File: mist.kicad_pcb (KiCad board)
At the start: 2 copper layers, 137 x 110 mm, 25 parts, among them SW1 SW_Push, SW10 SW_Push, SW11 SW_Push, SW12 SW_Push, SW13 SW_Push, SW14 SW_Push, SW15 SW_Push, SW16 SW_Push, SW17 SW_Push, SW18 SW_Push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

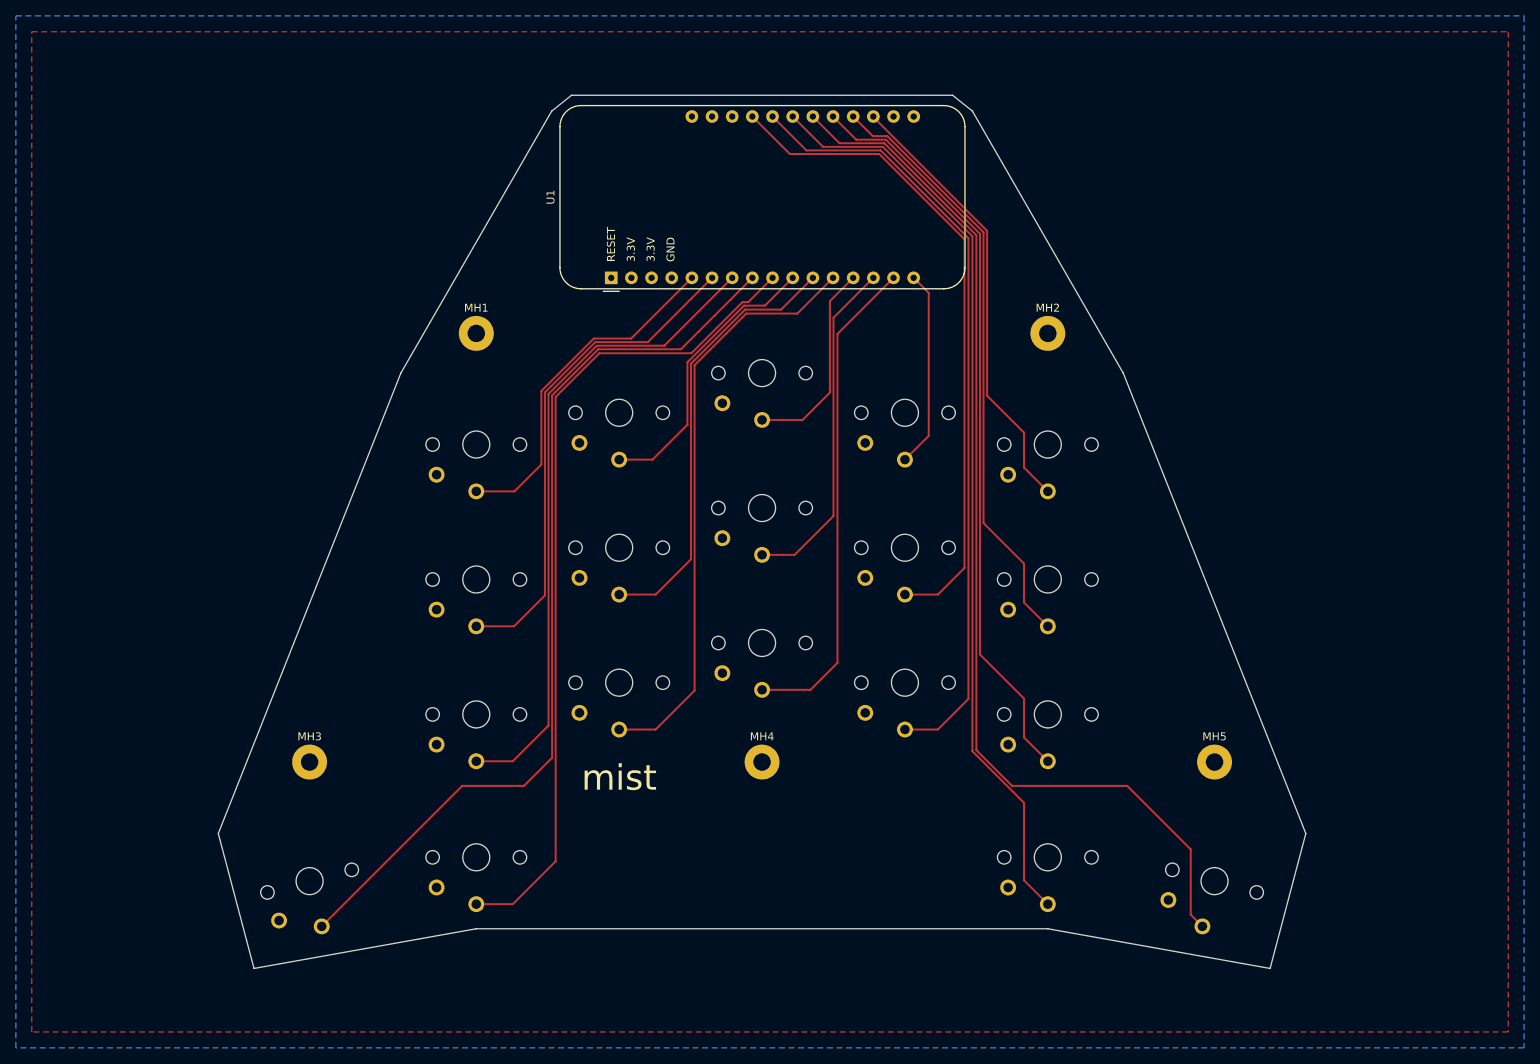
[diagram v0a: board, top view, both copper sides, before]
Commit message: added clickhole and gerbers
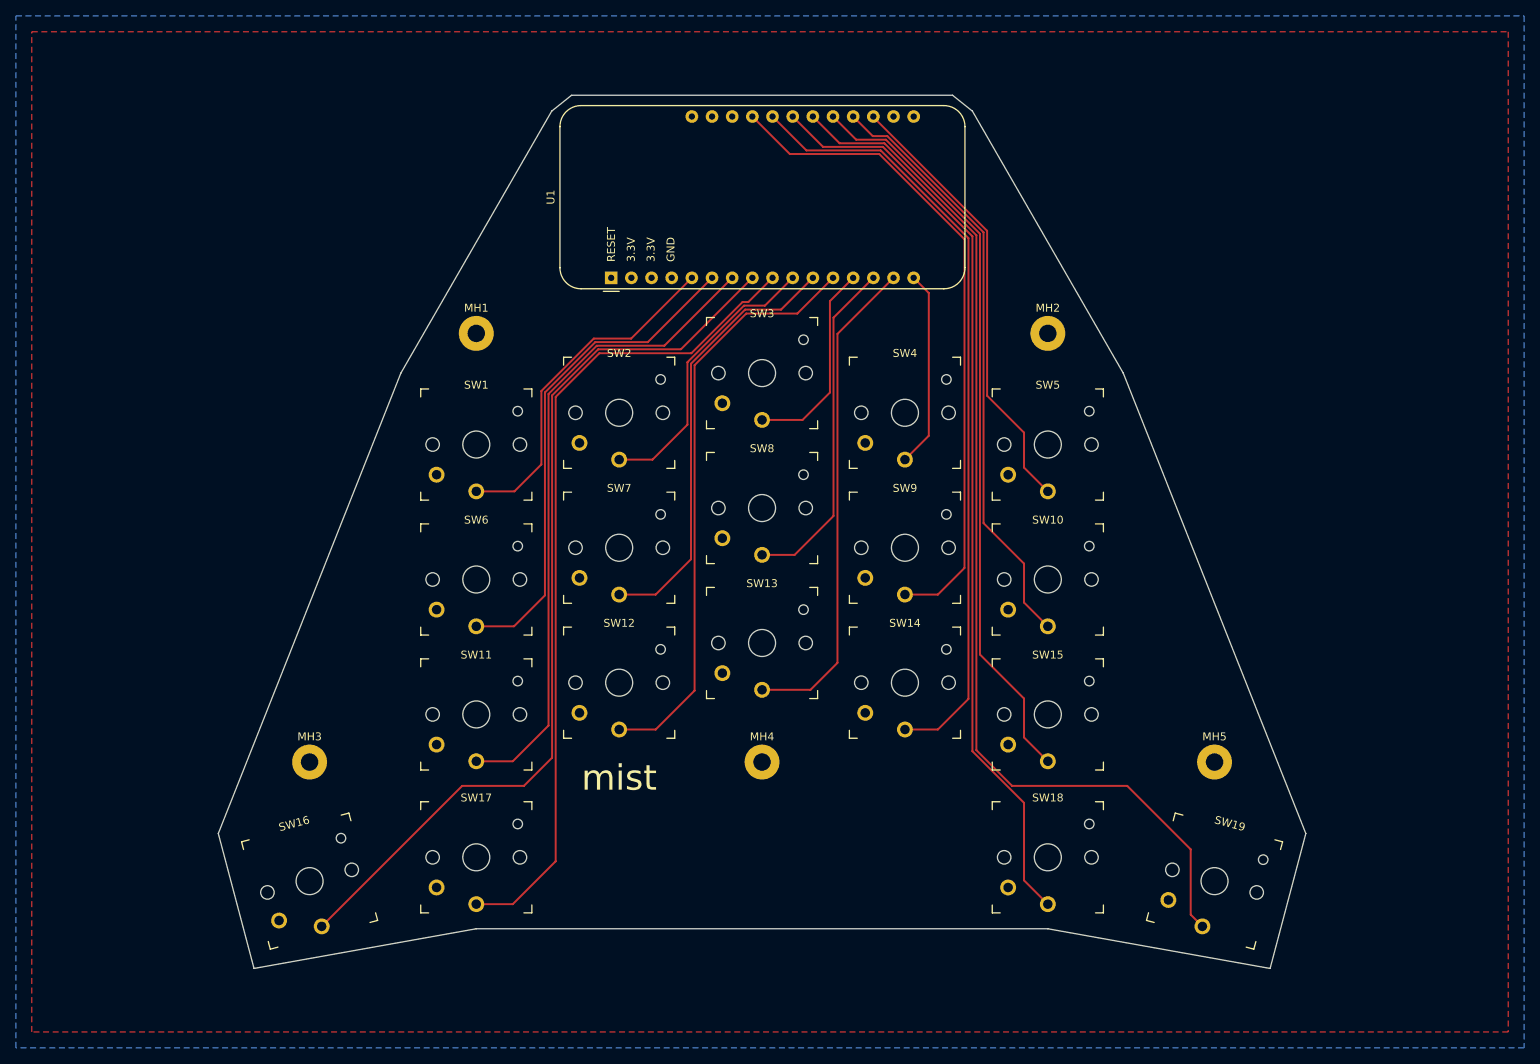
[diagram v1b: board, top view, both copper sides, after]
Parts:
- SW1, SW10, SW11, SW12, SW13, SW14, SW15, SW16, SW17, SW18, SW19, SW2, SW3, SW4, SW5, SW6, SW7, SW8, SW9: footprint Keebio-Parts:Kailh-PG1350-1u-NoLED -> Keebio-Parts:Kailh-PG1350-1u-Clickhole-NoLED
